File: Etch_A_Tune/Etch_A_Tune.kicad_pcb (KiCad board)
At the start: 2 copper layers, 116.5 x 101.7 mm, 141 parts, among them J1 75915-414LF, J2 91601-304ALF, J3 91601-304ALF, J4 2171790001, J5 SJ-3524-SMT-PI, J6 91601-304ALF, J7 3220-10-0300-00, U1 BQ297xy, U2 CSD16406Q3, U3 CSD16406Q3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

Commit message: Update
Added headers for ADC Pins and 4 extra GPIOs
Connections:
- U6 pad 10: (no net) -> GND
- U6 pad 11: (no net) -> GND
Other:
- board text added: "Team 07 Etch-A-Tune V1.0 11.19.2025"
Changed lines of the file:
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@@
 			(layers "*.Cu")
 			(remove_unused_layers no)
+			(net 22 "GND")
 		)
 		(pad "11" thru_hole circle
@@
 			(size 0.4 0.4)
 			(drill 0.2)
-			(layers "*.Cu" "B.Mask")
+			(layers "*.Cu" "B.Mask" "B.Adhes")
 			(remove_unused_layers no)
+			(net 22 "GND")
 		)
 		(embedded_fonts no)
@@
 		(layer "Edge.Cuts")
 	)
+	(gr_text "Team 07\nEtch-A-Tune\nV1.0\n11.19.2025"
+		(at 127.72714 98.74 0)
+		(layer "B.SilkS")
+		(effects
+			(font
+				(size 2 2)
+				(thickness 0.2)
+			)
+			(justify left bottom mirror)
+		)
+	)
 	(segment
 		(start 49.04 34.24)
@@
 	)
 	(zone
+		(net 42)
+		(net_name "/SCK")
+		(layer "F.Cu")
+		(name "$teardrop_padvia$")
+		(hatch none 0.1)
+		(priority 30008)
+		(attr
+			(teardrop
+				(type padvia)
+			)
+		)
+		(connect_pads yes
+			(clearance 0)
+		)
+		(min_thickness 0.0254)
+		(filled_areas_thickness no)
+		(fill yes
+			(thermal_gap 0.5)
+			(thermal_bridge_width 0.5)
+			(island_removal_mode 1)
+			(island_area_min 10)
+		)
+		(polygon
+			(pts
+				(xy 23.188471 52.64) (xy 23.188471 52.44) (xy 22.333342 52.041118) (xy 21.999 52.54) (xy 22.333342 53.038882)
+			)
+		)
+	)
+	(zone
+		(net 40)
+		(net_name "/T_DO")
+		(layer "F.Cu")
+		(name "$teardrop_padvia$")
+		(hatch none 0.1)
+		(priority 30010)
+		(attr
+			(teardrop
+				(type padvia)
+			)
+		)
+		(connect_pads yes
+			(clearance 0)
+		)
+		(min_thickness 0.0254)
+		(filled_areas_thickness no)
+		(fill yes
+			(thermal_gap 0.5)
+			(thermal_bridge_width 0.5)
+			(island_removal_mode 1)
+			(island_area_min 10)
+		)
+		(polygon
+			(pts
+				(xy 21.088914 38.069665) (xy 21.230335 38.211086) (xy 22.117054 37.888471) (xy 22.000707 37.299293)
+				(xy 21.411529 37.182946)
+			)
+		)
+	)
+	(zone
 		(net 22)
 		(net_name "GND")
@@
 	)
 	(zone
-		(net 35)
-		(net_name "/LED")
+		(net 33)
+		(net_name "/DC{slash}RS")
 		(layer "F.Cu")
 		(name "$teardrop_padvia$")
 		(hatch none 0.1)
-		(priority 30005)
+		(priority 30003)
 		(attr
 			(teardrop
@@
 		(polygon
 			(pts
-				(xy 23.188471 50.1) (xy 23.188471 49.9) (xy 22.333342 49.501118) (xy 21.999 50) (xy 22.333342 50.498882)
+				(xy 23.188471 57.72) (xy 23.188471 57.52) (xy 22.333342 57.121118) (xy 21.999 57.62) (xy 22.333342 58.118882)
 			)
 		)
 	)
 	(zone
-		(net 41)
-		(net_name "/CS")
+		(net 32)
+		(net_name "/SDI (MOSI)")
 		(layer "F.Cu")
 		(name "$teardrop_padvia$")
 		(hatch none 0.1)
-		(priority 30007)
+		(priority 30002)
 		(attr
 			(teardrop
@@
 		(polygon
 			(pts
-				(xy 23.188471 62.8) (xy 23.188471 62.6) (xy 22.333342 62.201118) (xy 21.999 62.7) (xy 22.333342 63.198882)
+				(xy 23.188471 55.18) (xy 23.188471 54.98) (xy 22.333342 54.581118) (xy 21.999 55.08) (xy 22.333342 55.578882)
 			)
 		)
@@
 	)
 	(zone
-		(net 38)
-		(net_name "/T_CS")
+		(net 37)
+		(net_name "/SDO(MISO)")
 		(layer "F.Cu")
 		(name "$teardrop_padvia$")
 		(hatch none 0.1)
-		(priority 30006)
+		(priority 30005)
 		(attr
 			(teardrop
@@
 		(polygon
 			(pts
-				(xy 23.188471 42.48) (xy 23.188471 42.28) (xy 22.333342 41.881118) (xy 21.999 42.38) (xy 22.333342 42.878882)
+				(xy 23.188471 47.56) (xy 23.188471 47.36) (xy 22.333342 46.961118) (xy 21.999 47.46) (xy 22.333342 47.958882)
 			)
 		)
 	)
 	(zone
-		(net 32)
-		(net_name "/SDI (MOSI)")
+		(net 38)
+		(net_name "/T_CS")
 		(layer "F.Cu")
 		(name "$teardrop_padvia$")
 		(hatch none 0.1)
-		(priority 30001)
+		(priority 30006)
 		(attr
 			(teardrop
@@
 		(polygon
 			(pts
-				(xy 23.188471 55.18) (xy 23.188471 54.98) (xy 22.333342 54.581118) (xy 21.999 55.08) (xy 22.333342 55.578882)
+				(xy 23.188471 42.48) (xy 23.188471 42.28) (xy 22.333342 41.881118) (xy 21.999 42.38) (xy 22.333342 42.878882)
 			)
 		)
@@
 	)
 	(zone
-		(net 40)
-		(net_name "/T_DO")
+		(net 34)
+		(net_name "/T_IRQ")
 		(layer "F.Cu")
 		(name "$teardrop_padvia$")
 		(hatch none 0.1)
-		(priority 30009)
+		(priority 30000)
 		(attr
 			(teardrop
@@
 		(polygon
 			(pts
-				(xy 21.088914 38.069665) (xy 21.230335 38.211086) (xy 22.117054 37.888471) (xy 22.000707 37.299293)
-				(xy 21.411529 37.182946)
+				(xy 22.1 33.56) (xy 21.9 33.56) (xy 21.4 34.16) (xy 22 34.761) (xy 22.6 34.16)
 			)
 		)
@@
 	)
 	(zone
-		(net 36)
-		(net_name "/T_CLK")
+		(net 41)
+		(net_name "/CS")
 		(layer "F.Cu")
 		(name "$teardrop_padvia$")
 		(hatch none 0.1)
-		(priority 30010)
+		(priority 30007)
 		(attr
 			(teardrop
@@
 		(polygon
 			(pts
-				(xy 21.088914 45.689665) (xy 21.230335 45.831086) (xy 22.117054 45.508471) (xy 22.000707 44.919293)
-				(xy 21.411529 44.802946)
+				(xy 23.188471 62.8) (xy 23.188471 62.6) (xy 22.333342 62.201118) (xy 21.999 62.7) (xy 22.333342 63.198882)
 			)
 		)
 	)
 	(zone
-		(net 39)
-		(net_name "/T_DIN")
+		(net 36)
+		(net_name "/T_CLK")
 		(layer "F.Cu")
 		(name "$teardrop_padvia$")
 		(hatch none 0.1)
-		(priority 30011)
+		(priority 30009)
 		(attr
 			(teardrop
@@
 		(polygon
 			(pts
-				(xy 20.916555 40.222024) (xy 21.057976 40.363445) (xy 21.882946 40.428471) (xy 22.000707 39.839293)
-				(xy 21.501118 39.506658)
+				(xy 21.088914 45.689665) (xy 21.230335 45.831086) (xy 22.117054 45.508471) (xy 22.000707 44.919293)
+				(xy 21.411529 44.802946)
 			)
 		)
 	)
 	(zone
-		(net 42)
-		(net_name "/SCK")
+		(net 39)
+		(net_name "/T_DIN")
 		(layer "F.Cu")
 		(name "$teardrop_padvia$")
 		(hatch none 0.1)
-		(priority 30008)
+		(priority 30011)
 		(attr
 			(teardrop
@@
 		(polygon
 			(pts
-				(xy 23.188471 52.64) (xy 23.188471 52.44) (xy 22.333342 52.041118) (xy 21.999 52.54) (xy 22.333342 53.038882)
+				(xy 20.916555 40.222024) (xy 21.057976 40.363445) (xy 21.882946 40.428471) (xy 22.000707 39.839293)
+				(xy 21.501118 39.506658)
 			)
 		)
 	)
 	(zone
-		(net 34)
-		(net_name "/T_IRQ")
+		(net 31)
+		(net_name "/RESET")
 		(layer "F.Cu")
 		(name "$teardrop_padvia$")
 		(hatch none 0.1)
-		(priority 30000)
+		(priority 30001)
 		(attr
 			(teardrop
@@
 		(polygon
 			(pts
-				(xy 22.1 33.56) (xy 21.9 33.56) (xy 21.4 34.16) (xy 22 34.761) (xy 22.6 34.16)
+				(xy 23.188471 60.26) (xy 23.188471 60.06) (xy 22.333342 59.661118) (xy 21.999 60.16) (xy 22.333342 60.658882)
 			)
 		)
 	)
 	(zone
-		(net 31)
-		(net_name "/RESET")
+		(net 10)
+		(net_name "Net-(U4-AVIN)")
 		(layer "F.Cu")
-		(name "$teardrop_padvia$")
-		(hatch none 0.1)
-		(priority 30002)
-		(attr
-			(teardrop
-				(type padvia)
-			)
-		)
+		(hatch edge 0.5)
+		(priority 2)
 		(connect_pads yes
-			(clearance 0)
+			(clearance 0.5)
 		)
-		(min_thickness 0.0254)
+		(min_thickness 0.25)
 		(filled_areas_thickness no)
 		(fill yes
 			(thermal_gap 0.5)
 			(thermal_bridge_width 0.5)
-			(island_removal_mode 1)
-			(island_area_min 10)
 		)
 		(polygon
 			(pts
-				(xy 23.188471 60.26) (xy 23.188471 60.06) (xy 22.333342 59.661118) (xy 21.999 60.16) (xy 22.333342 60.658882)
+				(xy 37.54 43.630625) (xy 38.430625 42.74) (xy 43.399375 42.74) (xy 44.29 43.630625) (xy 44.29 46.8025)
+				(xy 43.3525 47.74) (xy 38.4775 47.74) (xy 37.54 46.8025)
 			)
 		)
 	)
 	(zone
-		(net 10)
-		(net_name "Net-(U4-AVIN)")
+		(net 22)
+		(net_name "GND")
 		(layer "F.Cu")
 		(hatch edge 0.5)
-		(priority 2)
+		(priority 11)
 		(connect_pads yes
 			(clearance 0.5)
@@
 		(polygon
 			(pts
-				(xy 37.54 43.630625) (xy 38.430625 42.74) (xy 43.399375 42.74) (xy 44.29 43.630625) (xy 44.29 46.8025)
-				(xy 43.3525 47.74) (xy 38.4775 47.74) (xy 37.54 46.8025)
+				(xy 28.79 112.49) (xy 31.29 112.49) (xy 31.29 116.74) (xy 28.79 116.74)
 			)
 		)
 	)
 	(zone
-		(net 33)
-		(net_name "/DC{slash}RS")
+		(net 35)
+		(net_name "/LED")
 		(layer "F.Cu")
 		(name "$teardrop_padvia$")
@@
 		(polygon
 			(pts
-				(xy 23.188471 57.72) (xy 23.188471 57.52) (xy 22.333342 57.121118) (xy 21.999 57.62) (xy 22.333342 58.118882)
+				(xy 23.188471 50.1) (xy 23.188471 49.9) (xy 22.333342 49.501118) (xy 21.999 50) (xy 22.333342 50.498882)
 			)
 		)
 	)
 	(zone
-		(net 22)
-		(net_name "GND")
-		(layer "F.Cu")
+		(net 12)
+		(net_name "Net-(U1-VSS)")
+		(layer "B.Cu")
 		(hatch edge 0.5)
-		(priority 11)
-		(connect_pads yes
+		(priority 9)
+		(connect_pads
 			(clearance 0.5)
 		)
@@
 		(polygon
 			(pts
-				(xy 28.79 112.49) (xy 31.29 112.49) (xy 31.29 116.74) (xy 28.79 116.74)
+				(xy 121.54 32.24) (xy 125.54 35.74) (xy 125.54 48.115) (xy 121.415 52.24) (xy 98.79 52.24) (xy 95.04 48.49)
+				(xy 95.04 37.24) (xy 100.04 32.24)
 			)
 		)
 	)
 	(zone
-		(net 37)
-		(net_name "/SDO(MISO)")
-		(layer "F.Cu")
+		(net 34)
+		(net_name "/T_IRQ")
+		(layer "B.Cu")
 		(name "$teardrop_padvia$")
 		(hatch none 0.1)
-		(priority 30003)
+		(priority 30000)
 		(attr
 			(teardrop
@@
 		(polygon
 			(pts
-				(xy 23.188471 47.56) (xy 23.188471 47.36) (xy 22.333342 46.961118) (xy 21.999 47.46) (xy 22.333342 47.958882)
-			)
-		)
-	)
-	(zone
-		(net 12)
-		(net_name "Net-(U1-VSS)")
-		(layer "B.Cu")
-		(hatch edge 0.5)
-		(priority 9)
-		(connect_pads
-			(clearance 0.5)
-		)
-		(min_thickness 0.25)
-		(filled_areas_thickness no)
-		(fill yes
-			(thermal_gap 0.5)
-			(thermal_bridge_width 0.5)
-		)
-		(polygon
-			(pts
-				(xy 121.54 32.24) (xy 125.54 35.74) (xy 125.54 48.115) (xy 121.415 52.24) (xy 98.79 52.24) (xy 95.04 48.49)
-				(xy 95.04 37.24) (xy 100.04 32.24)
+				(xy 20.905026 35.713553) (xy 21.046447 35.854974) (xy 22.248528 35.36) (xy 22.000707 34.759293)
+				(xy 21.4 34.511472)
 			)
 		)
@@
 			)
 		)
-	)
-	(zone
-		(net 34)
-		(net_name "/T_IRQ")
-		(layer "B.Cu")
-		(name "$teardrop_padvia$")
-		(hatch none 0.1)
-		(priority 30000)
-		(attr
-			(teardrop
-				(type padvia)
-			)
-		)
-		(connect_pads yes
-			(clearance 0)
-		)
-		(min_thickness 0.0254)
-		(filled_areas_thickness no)
-		(fill yes
-			(thermal_gap 0.5)
-			(thermal_bridge_width 0.5)
-			(island_removal_mode 1)
-			(island_area_min 10)
-		)
-		(polygon
-			(pts
-				(xy 20.905026 35.713553) (xy 21.046447 35.854974) (xy 22.248528 35.36) (xy 22.000707 34.759293)
-				(xy 21.4 34.511472)
-			)
-		)

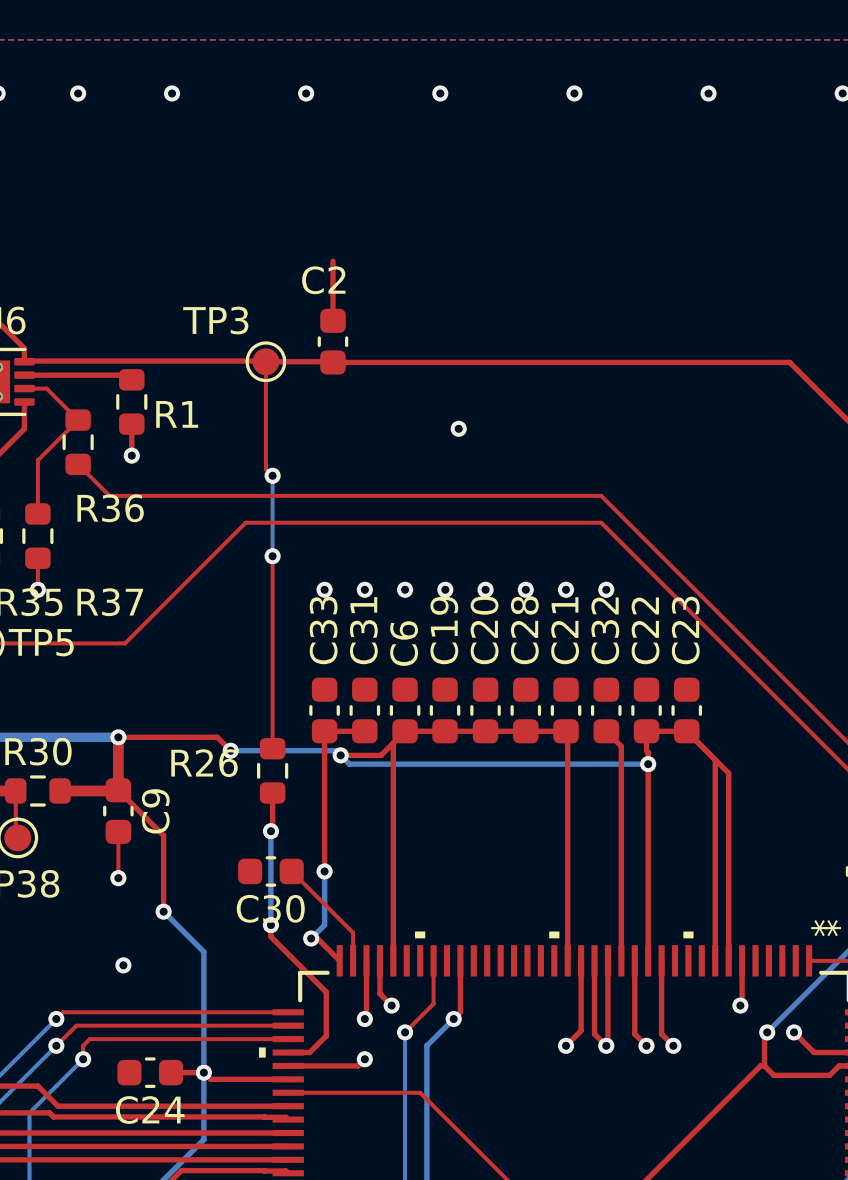
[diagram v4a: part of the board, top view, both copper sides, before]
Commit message: Finished PCB
Added ferrite bead and crystal oscillator. Added silkscreen text and tidied up component designators.
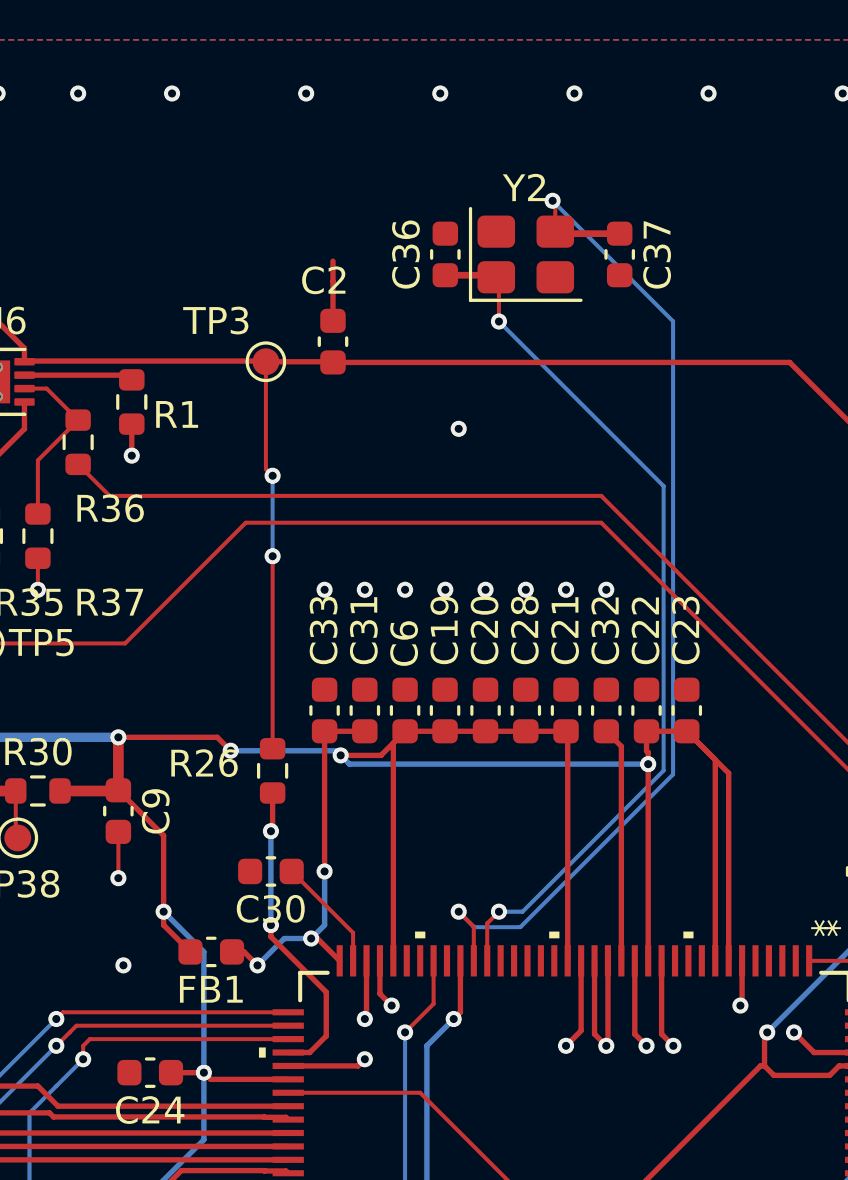
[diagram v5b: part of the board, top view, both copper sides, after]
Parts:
- added C36: 18pf, Capacitor_SMD:C_0603_1608Metric, F.Cu at (71.7, 29.2)
- added C37: 18pf, Capacitor_SMD:C_0603_1608Metric, F.Cu at (78.2, 29.2)
- added FB1: FerriteBead_Small, Capacitor_SMD:C_0603_1608Metric, F.Cu at (63.0, 55.2)
- added Y2: 12Mhz, Crystal:Crystal_SMD_Abracon_ABM8G-4Pin_3.2x2.5mm, F.Cu at (74.7, 29.2)
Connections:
- U5 pad 25: unconnected-(U5A-PH0-OSC_IN-Pad25) -> OSC_H_IN
- U5 pad 26: unconnected-(U5A-PH1-OSC_OUT-Pad26) -> OSC_H_OUT
- U6 pad 10: GND -> (no net)
- U6 pad 11: GND -> (no net)
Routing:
- net OSC_H_OUT: track 0.00 -> 39.7 mm, vias 0 -> 2
- net OSC_H_IN: track 0.00 -> 33.4 mm, vias 0 -> 2
- net Net-(U5A-VDDA): track 10.8 -> 14.4 mm, vias 2 -> 3
- net +3.3V: track 609.6 -> 611.5 mm

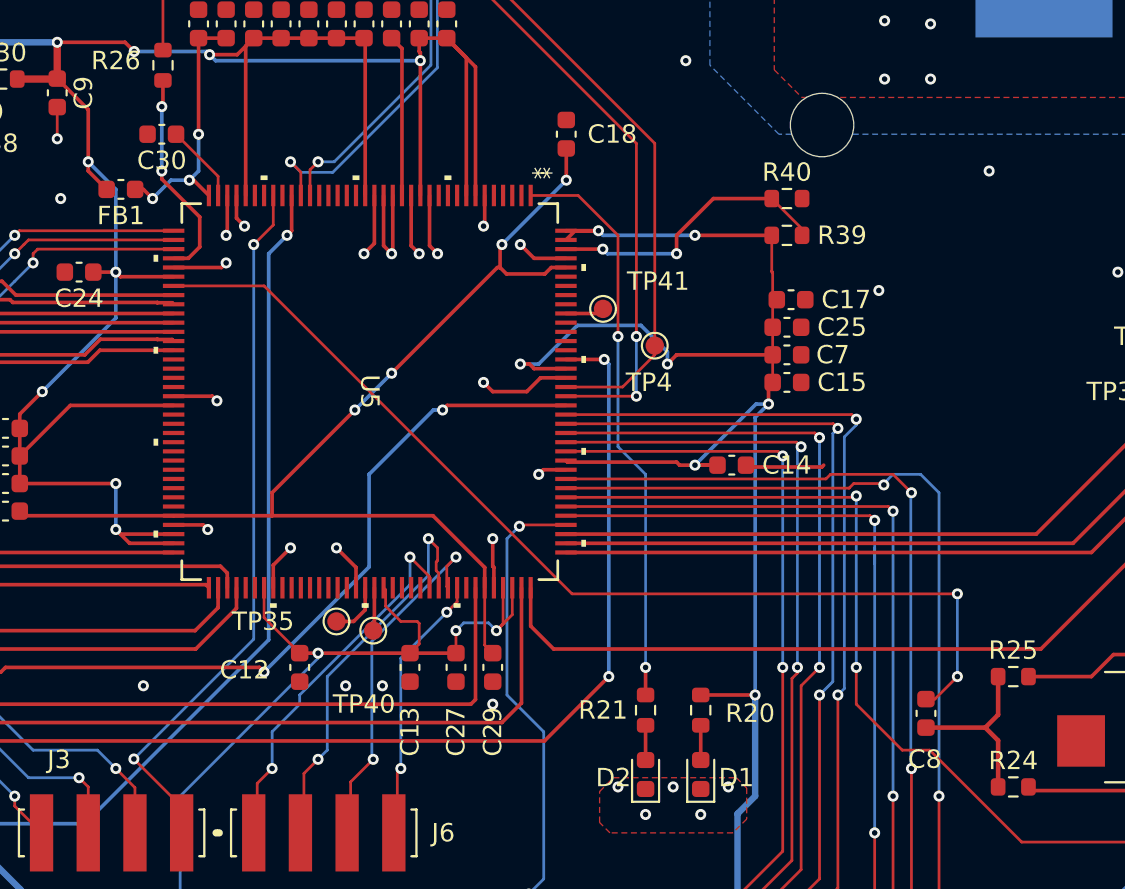
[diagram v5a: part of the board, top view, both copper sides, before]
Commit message: Update
Changed DC blocking cap to 1206 footprint, added SVG silkscreen to back of board and added team name date and version
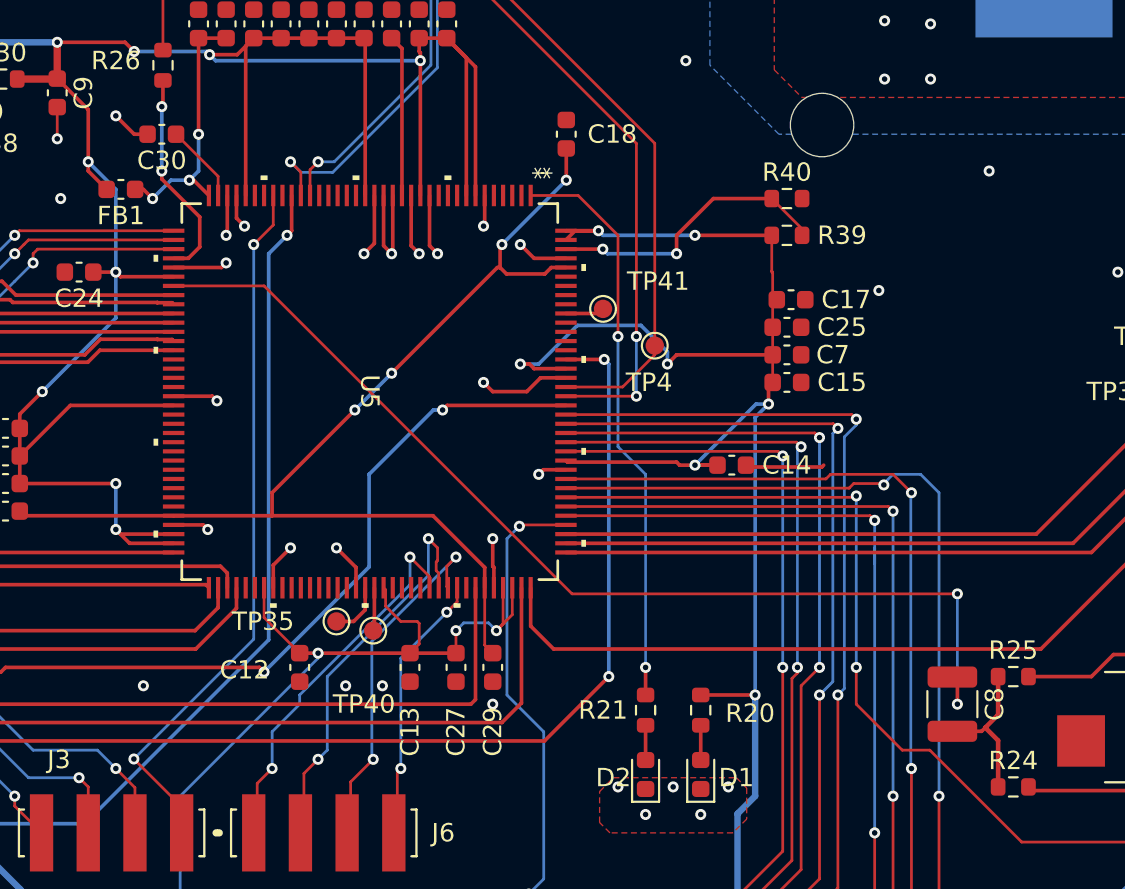
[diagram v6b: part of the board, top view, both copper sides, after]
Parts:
- C8: footprint Capacitor_SMD:C_0603_1608Metric -> Capacitor_SMD:C_1210_3225Metric
- moved C8 1.52 mm to (108.2, 83.2)
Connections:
- U6 pad 10: (no net) -> GND
- U6 pad 11: (no net) -> GND
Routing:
- net GND: track 79.6 -> 81.8 mm, vias 114 -> 115
- net Net-(C8-Pad2): track 9.80 -> 8.45 mm
- net /Microcontroller/DAC_OUT: track 56.3 -> 57.2 mm
